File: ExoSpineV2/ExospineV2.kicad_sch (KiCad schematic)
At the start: 10 parts, among them J1 GPIO, J19 Conn_01x03_Socket, J4 Conn_01x03_Socket, J5 Conn_01x04_Socket, U1 CAT24C256

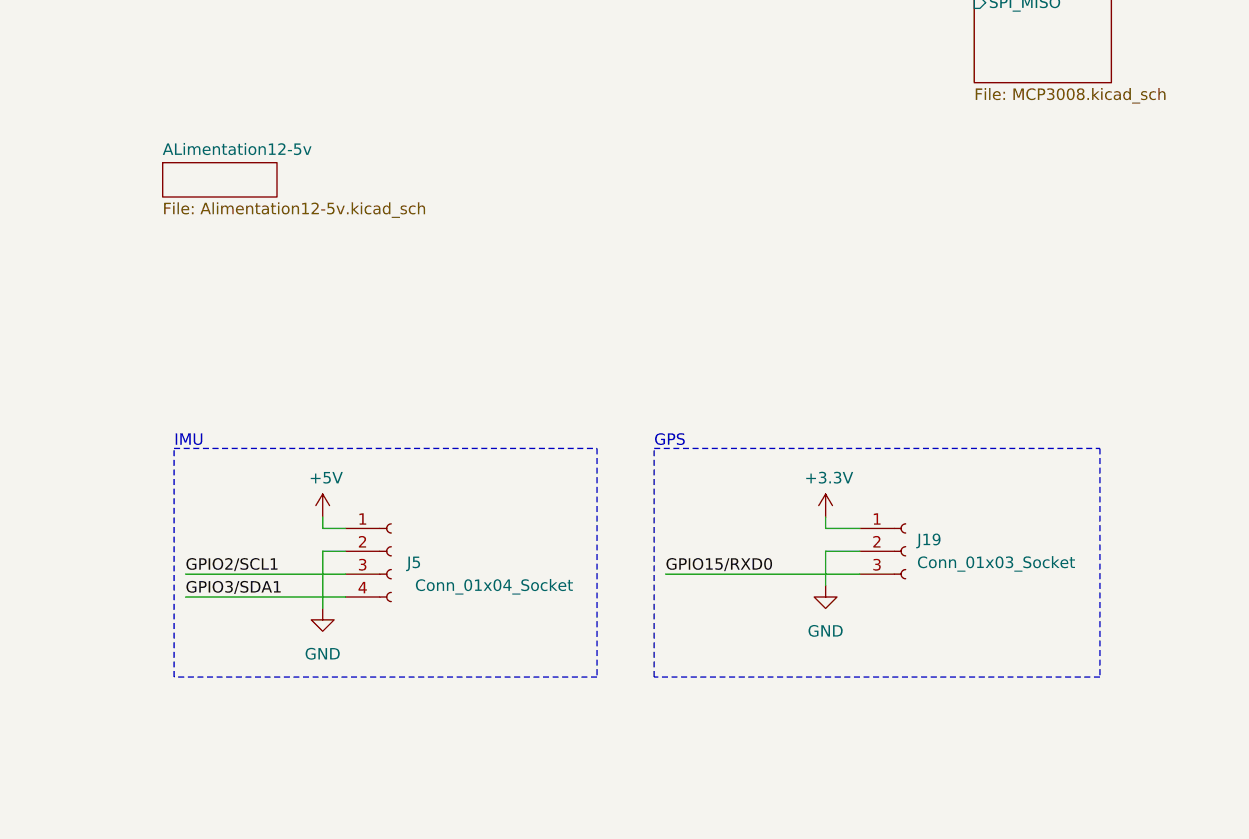
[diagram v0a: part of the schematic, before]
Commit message: ajout des capteurs de pression (x3) et d'un peu d'info sur le dcdc12-5v
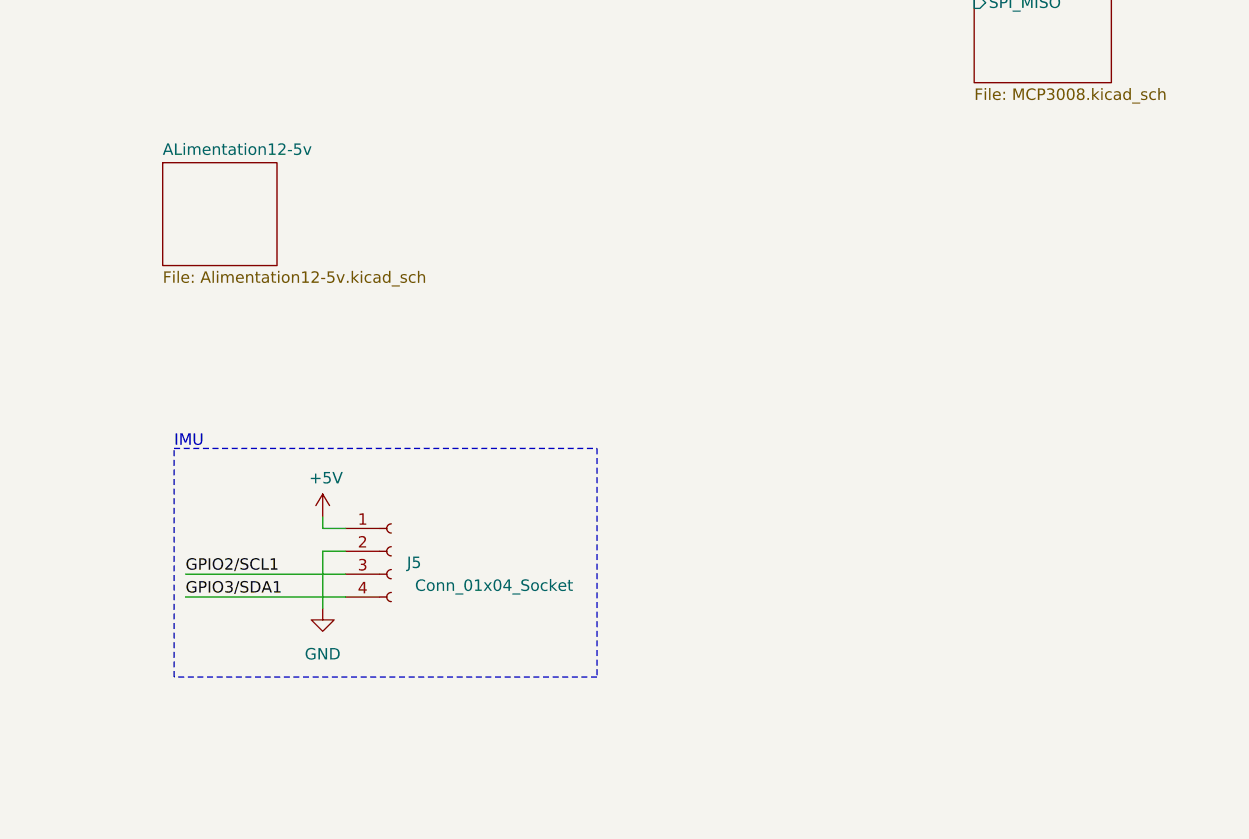
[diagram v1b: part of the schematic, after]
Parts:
- removed J19: Conn_01x03_Socket, symbol Connector:Conn_01x03_Socket
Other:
- note removed: "GPS"
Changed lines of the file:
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@@
     (stroke (width 0) (type solid))
-  )
-  (wire (pts (xy 232.41 116.84) (xy 236.22 116.84))
-    (stroke (width 0) (type default))
   )
   (wire (pts (xy 73.66 35.56) (xy 100.33 35.56))
@@
     (stroke (width 0) (type solid))
   )
-  (wire (pts (xy 214.63 121.92) (xy 236.22 121.92))
-    (stroke (width 0) (type default))
-  )
   (wire (pts (xy 76.2 68.58) (xy 73.66 68.58))
     (stroke (width 0) (type solid))
@@
     (stroke (width 0) (type solid))
   )
-  (wire (pts (xy 236.22 119.38) (xy 232.41 119.38))
-    (stroke (width 0) (type default))
-  )
   (wire (pts (xy 55.88 27.94) (xy 55.88 48.26))
     (stroke (width 0) (type solid))
@@
     (stroke (width 0) (type solid))
   )
-  (wire (pts (xy 232.41 115.57) (xy 232.41 116.84))
-    (stroke (width 0) (type default))
-  )
   (wire (pts (xy 31.75 71.12) (xy 60.96 71.12))
     (stroke (width 0) (type solid))
@@
   (wire (pts (xy 55.88 27.94) (xy 60.96 27.94))
     (stroke (width 0) (type solid))
-  )
-  (wire (pts (xy 232.41 119.38) (xy 232.41 123.19))
-    (stroke (width 0) (type default))
   )
   (wire (pts (xy 161.29 121.92) (xy 179.07 121.92))
@@
     (fill (type none))
   )
-  (rectangle (start 213.36 111.76) (end 213.36 111.76)
-    (stroke (width 0) (type default))
-    (fill (type none))
-  )
-  (rectangle (start 213.36 107.95) (end 262.89 133.35)
-    (stroke (width 0) (type dash))
-    (fill (type none))
-  )
   (text "Thermistances\n" (at 143.51 30.48 0)
     (effects (font (size 1.27 1.27)) (justify left bottom))
@@
     (effects (font (size 1.27 1.27)) (justify left bottom))
   )
-  (text "GPS" (at 213.36 107.95 0)
-    (effects (font (size 1.27 1.27)) (justify left bottom))
-  )
   (label "ID_SDA" (at 31.75 60.96 0) (fields_autoplaced)
-    (effects (font (size 1.27 1.27)) (justify left bottom))
-  )
-  (label "GPIO15{slash}RXD0" (at 214.63 121.92 0) (fields_autoplaced)
     (effects (font (size 1.27 1.27)) (justify left bottom))
   )
@@
     )
   )
-  (symbol (lib_id "Connector:Conn_01x03_Socket") (at 241.3 119.38 0) (unit 1)
-    (in_bom yes) (on_board yes) (dnp no)
-    (property "Reference" "J19" (at 242.57 118.11 0)
-      (effects (font (size 1.27 1.27)) (justify left))
-    )
-    (property "Value" "Conn_01x03_Socket" (at 242.57 120.65 0)
-      (effects (font (size 1.27 1.27)) (justify left))
-    )
-    (property "Footprint" "" (at 241.3 119.38 0)
-      (effects (font (size 1.27 1.27)) hide)
-    )
-    (property "Datasheet" "~" (at 241.3 119.38 0)
-      (effects (font (size 1.27 1.27)) hide)
-    )
-    (pin "3")
-    (pin "2")
-    (pin "1")
-    (instances
-      (project "ExospineV2"
-        (path "/e63e39d7-6ac0-4ffd-8aa3-1841a4541b55"
-          (reference "J19") (unit 1)
-        )
-      )
-    )
-  )
   (symbol (lib_id "Connector:Conn_01x03_Socket") (at 165.1 40.64 0) (unit 1)
     (in_bom yes) (on_board yes) (dnp no) (fields_autoplaced)
@@
     )
   )
-  (symbol (lib_name "GND_3") (lib_id "power:GND") (at 232.41 123.19 0) (unit 1)
-    (in_bom yes) (on_board yes) (dnp no) (fields_autoplaced)
-    (property "Reference" "#PWR011" (at 232.41 129.54 0)
-      (effects (font (size 1.27 1.27)) hide)
-    )
-    (property "Value" "GND" (at 232.41 128.27 0)
-      (effects (font (size 1.27 1.27)))
-    )
-    (property "Footprint" "" (at 232.41 123.19 0)
-      (effects (font (size 1.27 1.27)) hide)
-    )
-    (property "Datasheet" "" (at 232.41 123.19 0)
-      (effects (font (size 1.27 1.27)) hide)
-    )
-    (pin "1")
-    (instances
-      (project "ExospineV2"
-        (path "/e63e39d7-6ac0-4ffd-8aa3-1841a4541b55"
-          (reference "#PWR011") (unit 1)
-        )
-      )
-    )
-  )
   (symbol (lib_id "power:+3.3V") (at 134.62 38.1 0) (unit 1)
     (in_bom yes) (on_board yes) (dnp no)
@@
     )
   )
-  (symbol (lib_id "power:+3.3V") (at 232.41 115.57 0) (unit 1)
-    (in_bom yes) (on_board yes) (dnp no)
-    (property "Reference" "#PWR013" (at 232.41 119.38 0)
-      (effects (font (size 1.27 1.27)) hide)
-    )
-    (property "Value" "+3.3V" (at 232.7783 111.2456 0)
-      (effects (font (size 1.27 1.27)))
-    )
-    (property "Footprint" "" (at 232.41 115.57 0)
-      (effects (font (size 1.27 1.27)))
-    )
-    (property "Datasheet" "" (at 232.41 115.57 0)
-      (effects (font (size 1.27 1.27)))
-    )
-    (pin "1")
-    (instances
-      (project "ExospineV2"
-        (path "/e63e39d7-6ac0-4ffd-8aa3-1841a4541b55"
-          (reference "#PWR013") (unit 1)
-        )
-      )
-    )
-  )
   (symbol (lib_id "power:+3.3V") (at 101.6 180.34 270) (unit 1)
     (in_bom yes) (on_board yes) (dnp no)
@@
     )
   )
-  (sheet (at 158.75 76.2) (size 12.7 3.81) (fields_autoplaced)
+  (sheet (at 158.75 76.2) (size 12.7 11.43) (fields_autoplaced)
     (stroke (width 0.1524) (type solid))
     (fill (color 0 0 0 0.0000))
@@
       (effects (font (size 1.27 1.27)) (justify left bottom))
     )
-    (property "Sheetfile" "Alimentation12-5v.kicad_sch" (at 158.75 80.5946 0)
+    (property "Sheetfile" "Alimentation12-5v.kicad_sch" (at 158.75 88.2146 0)
       (effects (font (size 1.27 1.27)) (justify left top))
     )

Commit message: probablement pas de grandes modifications
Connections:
- net GPIO17/SDA1 is gone; now on net GPIO17: J4.2 (Pin_2), R3.2
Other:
- sheet MCP3008 renamed Analog-Digital
- sheet Analog-Digital ports: added CS/SHDN, SPI_MOSI, SPI_SClK; removed none
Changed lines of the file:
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@@
+    (stroke (width 0) (type default))
+  )
+  (wire (pts (xy 22.86 119.38) (xy 52.07 119.38))
     (stroke (width 0) (type default))
   )
@@
     (stroke (width 0) (type default))
   )
+  (wire (pts (xy 22.86 114.3) (xy 52.07 114.3))
+    (stroke (width 0) (type solid))
+  )
   (wire (pts (xy 31.75 55.88) (xy 60.96 55.88))
     (stroke (width 0) (type solid))
@@
     (stroke (width 0) (type solid))
   )
+  (wire (pts (xy 52.07 111.76) (xy 22.86 111.76))
+    (stroke (width 0) (type solid))
+  )
   (wire (pts (xy 91.44 177.8) (xy 101.6 177.8))
     (stroke (width 0) (type solid))
@@
   )
   (wire (pts (xy 73.66 73.66) (xy 100.33 73.66))
+    (stroke (width 0) (type solid))
+  )
+  (wire (pts (xy 22.86 116.84) (xy 52.07 116.84))
     (stroke (width 0) (type solid))
   )
@@
     (effects (font (size 1.27 1.27)) (justify left bottom))
   )
+  (label "GPIO9{slash}SPI0.MISO" (at 22.86 114.3 0) (fields_autoplaced)
+    (effects (font (size 1.27 1.27)) (justify left bottom))
+  )
   (label "ID_SDA" (at 110.49 175.26 180) (fields_autoplaced)
     (effects (font (size 1.27 1.27)) (justify right bottom))
@@
     (effects (font (size 1.27 1.27)) (justify right bottom))
   )
-  (label "GPIO17{slash}SDA1" (at 132.08 49.53 0) (fields_autoplaced)
+  (label "GPIO17" (at 132.08 49.53 0) (fields_autoplaced)
     (effects (font (size 1.27 1.27)) (justify left bottom))
   )
@@
     (effects (font (size 1.27 1.27)) (justify right bottom))
   )
+  (label "GPIO25" (at 22.86 119.38 0) (fields_autoplaced)
+    (effects (font (size 1.27 1.27)) (justify left bottom))
+  )
+  (label "GPIO10{slash}SPI0.MOSI" (at 22.86 111.76 0) (fields_autoplaced)
+    (effects (font (size 1.27 1.27)) (justify left bottom))
+  )
   (label "GPIO22" (at 31.75 45.72 0) (fields_autoplaced)
+    (effects (font (size 1.27 1.27)) (justify left bottom))
+  )
+  (label "GPIO11{slash}SPI0.SCLK" (at 22.86 116.84 0) (fields_autoplaced)
     (effects (font (size 1.27 1.27)) (justify left bottom))
   )
@@
     )
   )
-  (sheet (at 158.75 76.2) (size 12.7 11.43) (fields_autoplaced)
+  (sheet (at 193.04 34.29) (size 13.97 12.7) (fields_autoplaced)
     (stroke (width 0.1524) (type solid))
     (fill (color 0 0 0 0.0000))
-    (property "Sheetname" "ALimentation12-5v" (at 158.75 75.4884 0)
+    (property "Sheetname" "ALimentation12-5v" (at 193.04 33.5784 0)
       (effects (font (size 1.27 1.27)) (justify left bottom))
     )
-    (property "Sheetfile" "Alimentation12-5v.kicad_sch" (at 158.75 88.2146 0)
+    (property "Sheetfile" "Alimentation12-5v.kicad_sch" (at 193.04 47.5746 0)
       (effects (font (size 1.27 1.27)) (justify left top))
     )
@@
     )
   )
-  (sheet (at 35.56 90.17) (size 12.7 3.81) (fields_autoplaced)
+  (sheet (at 193.04 55.88) (size 13.97 3.81) (fields_autoplaced)
     (stroke (width 0.1524) (type solid))
     (fill (color 0 0 0 0.0000))
-    (property "Sheetname" "ExoSpineV1" (at 35.56 89.4584 0)
+    (property "Sheetname" "ExoSpineV1" (at 193.04 55.1684 0)
       (effects (font (size 1.27 1.27)) (justify left bottom))
     )
-    (property "Sheetfile" "ExoSpineV1.kicad_sch" (at 35.56 94.5646 0)
+    (property "Sheetfile" "ExoSpineV1.kicad_sch" (at 193.04 60.2746 0)
       (effects (font (size 1.27 1.27)) (justify left top))
     )
@@
     )
   )
-  (sheet (at 248.92 55.88) (size 15.24 11.43) (fields_autoplaced)
+  (sheet (at 52.07 109.22) (size 17.78 11.43) (fields_autoplaced)
     (stroke (width 0.1524) (type solid))
     (fill (color 0 0 0 0.0000))
-    (property "Sheetname" "MCP3008" (at 248.92 55.1684 0)
+    (property "Sheetname" "Analog-Digital" (at 52.07 108.5084 0)
       (effects (font (size 1.27 1.27)) (justify left bottom))
     )
-    (property "Sheetfile" "MCP3008.kicad_sch" (at 248.92 67.8946 0)
+    (property "Sheetfile" "MCP3008.kicad_sch" (at 52.07 121.2346 0)
       (effects (font (size 1.27 1.27)) (justify left top))
     )
-    (pin "SPI_MISO" input (at 248.92 58.42 180)
-      (effects (font (size 1.27 1.27)) (justify left))
-    )
+    (pin "SPI_MISO" input (at 52.07 114.3 180)
+      (effects (font (size 1.27 1.27)) (justify left))
+    )
+    (pin "SPI_SClK" input (at 52.07 116.84 180)
+      (effects (font (size 1.27 1.27)) (justify left))
+    )
+    (pin "SPI_MOSI" input (at 52.07 111.76 180)
+      (effects (font (size 1.27 1.27)) (justify left))
+    )
+    (pin "CS{slash}SHDN" input (at 52.07 119.38 180)
+      (effects (font (size 1.27 1.27)) (justify left))
+    )

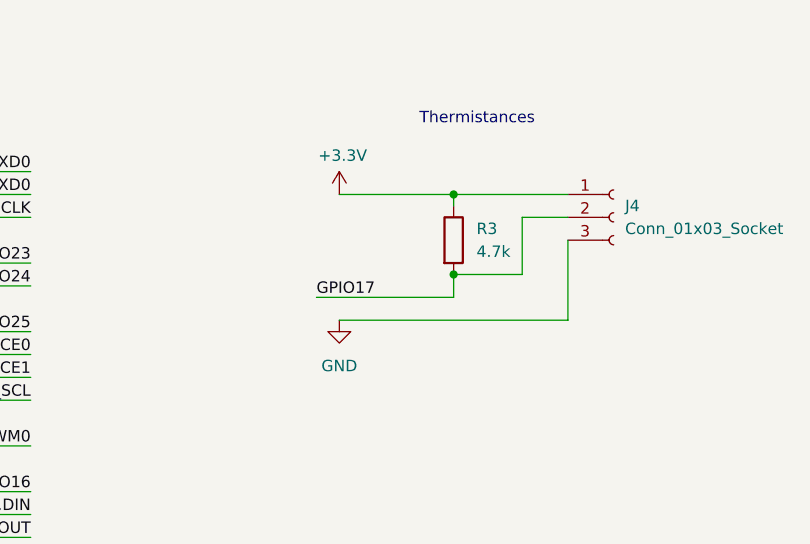
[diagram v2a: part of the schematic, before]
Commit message: ajout de condensateur de decouplage pour les thermistances
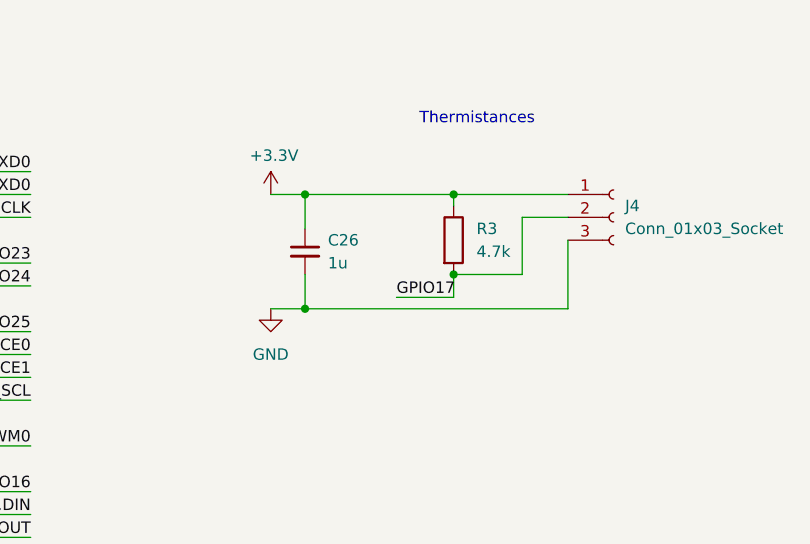
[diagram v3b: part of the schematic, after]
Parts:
- added C26: 1u, symbol Device:C_Small
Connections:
- net +3V3: now also C26.1
- net GND: now also C26.2
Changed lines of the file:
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@@
   (junction (at 101.6 165.1) (diameter 1.016) (color 0 0 0 0)
   )
+  (junction (at 130.81 38.1) (diameter 0) (color 0 0 0 0)
+  )
   (junction (at 58.42 76.2) (diameter 1.016) (color 0 0 0 0)
   )
@@
   )
   (junction (at 101.6 177.8) (diameter 1.016) (color 0 0 0 0)
+  )
+  (junction (at 130.81 50.8) (diameter 0) (color 0 0 0 0)
   )
   (junction (at 55.88 27.94) (diameter 1.016) (color 0 0 0 0)
@@
     (stroke (width 0) (type default))
   )
+  (wire (pts (xy 130.81 38.1) (xy 130.81 41.91))
+    (stroke (width 0) (type default))
+  )
   (wire (pts (xy 147.32 46.99) (xy 154.94 46.99))
     (stroke (width 0) (type default))
@@
     (stroke (width 0) (type solid))
   )
+  (wire (pts (xy 130.81 50.8) (xy 160.02 50.8))
+    (stroke (width 0) (type default))
+  )
   (wire (pts (xy 58.42 58.42) (xy 60.96 58.42))
     (stroke (width 0) (type solid))
@@
     (stroke (width 0) (type solid))
   )
-  (wire (pts (xy 134.62 52.07) (xy 160.02 52.07))
+  (wire (pts (xy 127 50.8) (xy 130.81 50.8))
     (stroke (width 0) (type default))
   )
@@
     (stroke (width 0) (type solid))
   )
-  (wire (pts (xy 134.62 38.1) (xy 147.32 38.1))
+  (wire (pts (xy 127 38.1) (xy 130.81 38.1))
     (stroke (width 0) (type default))
   )
@@
     (stroke (width 0) (type solid))
   )
+  (wire (pts (xy 130.81 46.99) (xy 130.81 50.8))
+    (stroke (width 0) (type default))
+  )
   (wire (pts (xy 76.2 24.13) (xy 76.2 27.94))
     (stroke (width 0) (type solid))
@@
     (stroke (width 0) (type default))
   )
-  (wire (pts (xy 160.02 43.18) (xy 160.02 52.07))
+  (wire (pts (xy 160.02 43.18) (xy 160.02 50.8))
     (stroke (width 0) (type default))
   )
@@
     (stroke (width 0) (type default))
   )
+  (wire (pts (xy 130.81 38.1) (xy 147.32 38.1))
+    (stroke (width 0) (type default))
+  )
   (wire (pts (xy 67.31 165.1) (xy 67.31 175.26))
     (stroke (width 0) (type solid))
@@
     (stroke (width 0) (type solid))
   )
-  (wire (pts (xy 132.08 49.53) (xy 147.32 49.53))
+  (wire (pts (xy 140.97 49.53) (xy 147.32 49.53))
     (stroke (width 0) (type default))
   )
@@
     (effects (font (size 1.27 1.27)) (justify right bottom))
   )
-  (label "GPIO17" (at 132.08 49.53 0) (fields_autoplaced)
+  (label "GPIO17" (at 140.97 49.53 0) (fields_autoplaced)
     (effects (font (size 1.27 1.27)) (justify left bottom))
   )
@@
     )
   )
-  (symbol (lib_name "GND_1") (lib_id "power:GND") (at 134.62 52.07 0) (unit 1)
+  (symbol (lib_name "GND_1") (lib_id "power:GND") (at 127 50.8 0) (unit 1)
     (in_bom yes) (on_board yes) (dnp no) (fields_autoplaced)
-    (property "Reference" "#PWR05" (at 134.62 58.42 0)
-      (effects (font (size 1.27 1.27)) hide)
-    )
-    (property "Value" "GND" (at 134.62 57.15 0)
-      (effects (font (size 1.27 1.27)))
-    )
-    (property "Footprint" "" (at 134.62 52.07 0)
-      (effects (font (size 1.27 1.27)) hide)
-    )
-    (property "Datasheet" "" (at 134.62 52.07 0)
+    (property "Reference" "#PWR05" (at 127 57.15 0)
+      (effects (font (size 1.27 1.27)) hide)
+    )
+    (property "Value" "GND" (at 127 55.88 0)
+      (effects (font (size 1.27 1.27)))
+    )
+    (property "Footprint" "" (at 127 50.8 0)
+      (effects (font (size 1.27 1.27)) hide)
+    )
+    (property "Datasheet" "" (at 127 50.8 0)
       (effects (font (size 1.27 1.27)) hide)
     )
@@
     )
   )
-  (symbol (lib_id "power:+3.3V") (at 134.62 38.1 0) (unit 1)
-    (in_bom yes) (on_board yes) (dnp no)
-    (property "Reference" "#PWR06" (at 134.62 41.91 0)
-      (effects (font (size 1.27 1.27)) hide)
-    )
-    (property "Value" "+3.3V" (at 134.9883 33.7756 0)
-      (effects (font (size 1.27 1.27)))
-    )
-    (property "Footprint" "" (at 134.62 38.1 0)
-      (effects (font (size 1.27 1.27)))
-    )
-    (property "Datasheet" "" (at 134.62 38.1 0)
+  (symbol (lib_id "power:+3.3V") (at 127 38.1 0) (unit 1)
+    (in_bom yes) (on_board yes) (dnp no)
+    (property "Reference" "#PWR06" (at 127 41.91 0)
+      (effects (font (size 1.27 1.27)) hide)
+    )
+    (property "Value" "+3.3V" (at 127.3683 33.7756 0)
+      (effects (font (size 1.27 1.27)))
+    )
+    (property "Footprint" "" (at 127 38.1 0)
+      (effects (font (size 1.27 1.27)))
+    )
+    (property "Datasheet" "" (at 127 38.1 0)
       (effects (font (size 1.27 1.27)))
     )
@@
         )
       )
+    )
+  )
+  (symbol (lib_id "Device:C_Small") (at 130.81 44.45 0) (unit 1)
+    (in_bom yes) (on_board yes) (dnp no) (fields_autoplaced)
+    (property "Reference" "C26" (at 133.35 43.1863 0)
+      (effects (font (size 1.27 1.27)) (justify left))
+    )
+    (property "Value" "1u" (at 133.35 45.7263 0)
+      (effects (font (size 1.27 1.27)) (justify left))
+    )
+    (property "Footprint" "" (at 130.81 44.45 0)
+      (effects (font (size 1.27 1.27)) hide)
+    )
+    (property "Datasheet" "~" (at 130.81 44.45 0)
+      (effects (font (size 1.27 1.27)) hide)
+    )
+    (pin "1")
+    (pin "2")
+    (instances
+      (project "ExospineV2"
+        (path "/e63e39d7-6ac0-4ffd-8aa3-1841a4541b55"
+          (reference "C26") (unit 1)
+        )
+      )
